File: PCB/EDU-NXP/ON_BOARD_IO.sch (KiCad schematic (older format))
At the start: 44 parts, among them Q1 2N7002, Q10 2N7002, Q3 2N7002, Q4 2N7002, Q5 2N7002, Q9 2N7002, SW1 TEC_1, SW2 TEC_2, SW3 TEC_3, SW4 TEC_4

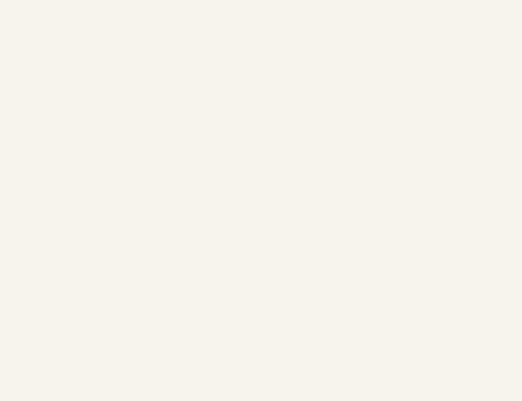
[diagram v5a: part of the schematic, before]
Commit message: PCB V0.0 finalizado - Se agregaron planos de masa, control de dimensiones y perforaciones, se agregó el LOGO
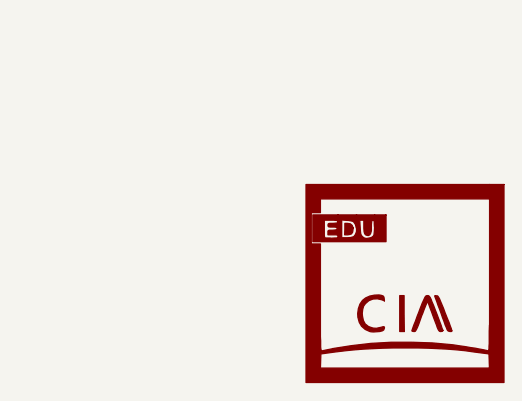
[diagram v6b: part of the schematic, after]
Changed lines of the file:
@@
 LIBS:pbss5240xf
 LIBS:LED_RGB
+LIBS:Logo
 LIBS:edu-ciaa-nxp-cache
 EELAYER 27 0
@@
 Sheet 6 7
 Title "EDU CIAA EXPANSIÓN"
-Date "12 jul 2014"
+Date "14 jul 2014"
 Rev ""
 Comp ""
@@
 	1    0    0    -1
 $EndComp
+$Comp
+L LOGO #G6
+U 1 1 53C3FC66
+P 10550 6550
+F 0 "#G6" H 10550 6147 60  0001 C CNN
+F 1 "LOGO" H 10550 6953 60  0001 C CNN
+F 2 "" H 10550 6550 60  0000 C CNN
+F 3 "" H 10550 6550 60  0000 C CNN
+	1    10550 6550
+	1    0    0    -1
+$EndComp

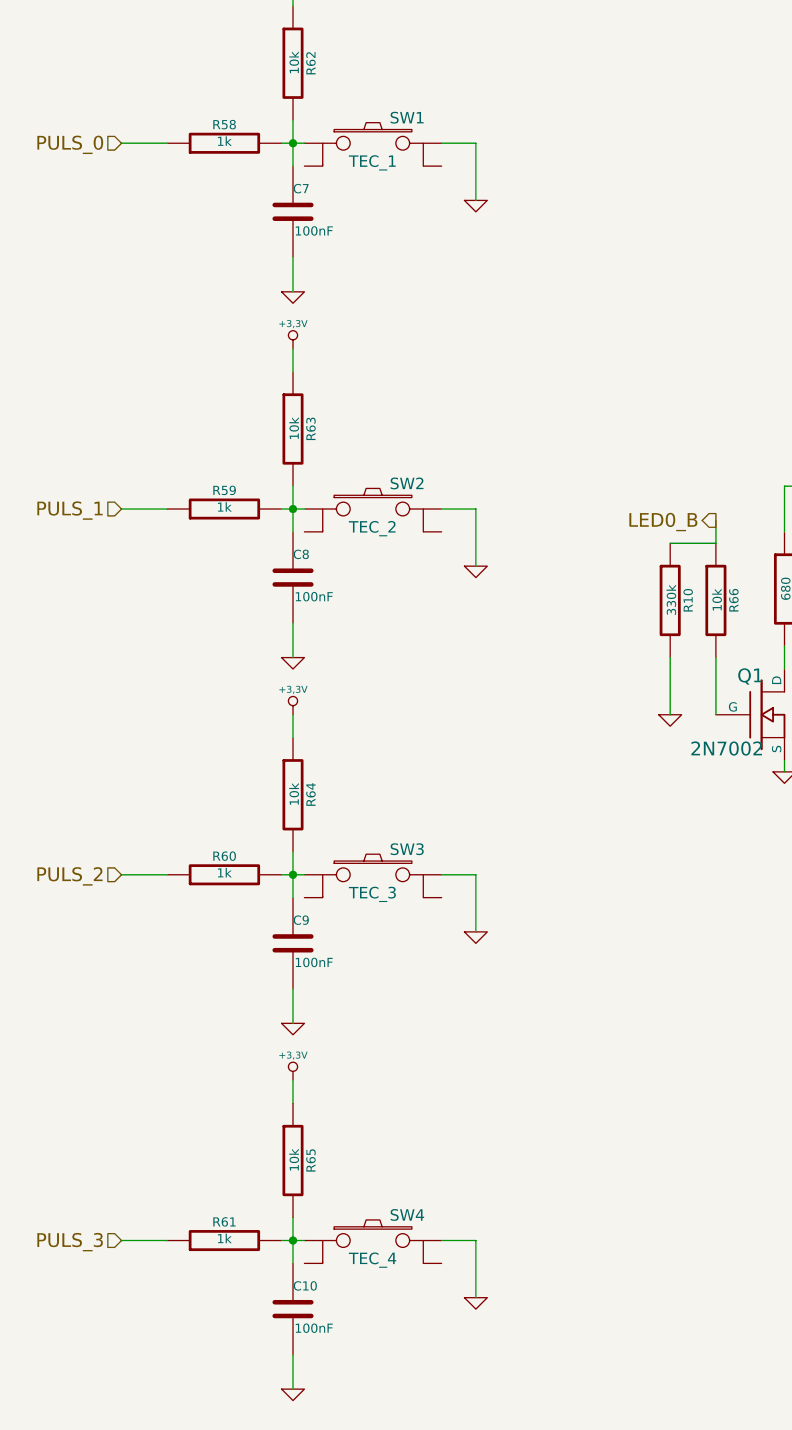
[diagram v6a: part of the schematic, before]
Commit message: Teclas THT y conectores micro USB THT
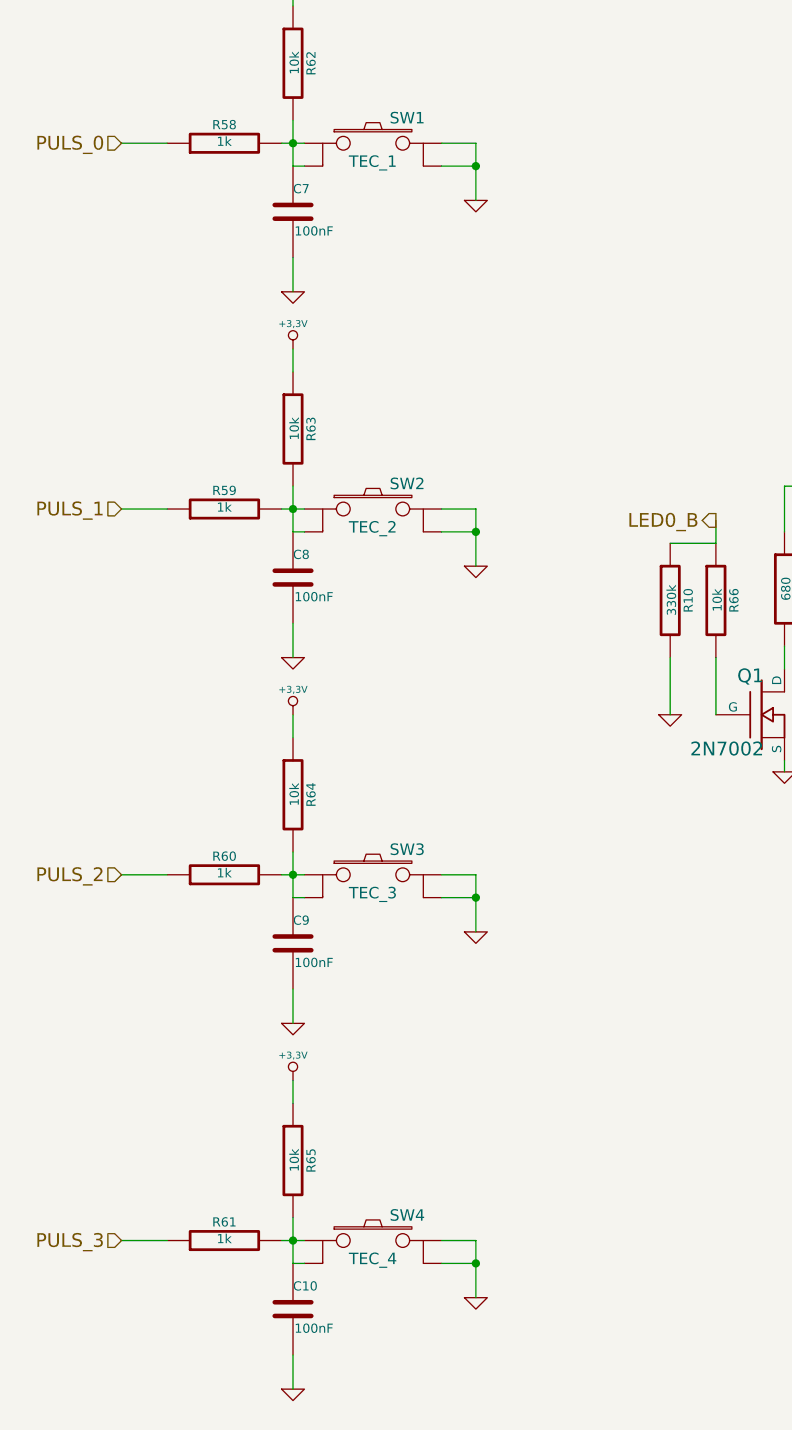
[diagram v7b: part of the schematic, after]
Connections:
- net GND: now also SW1.4, SW2.4, SW3.4, SW4.4
- net at C7.1, R58.2, R62.2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: now also SW1.2
- net at C8.1, R59.2, R63.2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: now also SW2.2
- net at C9.1, R60.2, R64.2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: now also SW3.2
- net at C10.1, R61.2, R65.2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: now also SW4.2
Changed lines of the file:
@@
 LIBS:LED_RGB
 LIBS:Logo
+LIBS:edu-ciaa-logo
 LIBS:edu-ciaa-nxp-cache
 EELAYER 27 0
@@
 Sheet 6 7
 Title "EDU CIAA EXPANSIÓN"
-Date "14 jul 2014"
+Date "17 jul 2014"
 Rev ""
 Comp ""
@@
 	1    0    0    -1
 $EndComp
+Wire Wire Line
+	1900 1500 1950 1500
+Wire Wire Line
+	2550 1500 2700 1500
+Connection ~ 2700 1500
+Wire Wire Line
+	1900 3100 1950 3100
+Wire Wire Line
+	2550 3100 2700 3100
+Connection ~ 2700 3100
+Wire Wire Line
+	1900 4700 1950 4700
+Wire Wire Line
+	2550 4700 2700 4700
+Connection ~ 2700 4700
+Wire Wire Line
+	1900 6300 1950 6300
+Wire Wire Line
+	2550 6300 2700 6300
+Connection ~ 2700 6300
 $EndSCHEMATC
